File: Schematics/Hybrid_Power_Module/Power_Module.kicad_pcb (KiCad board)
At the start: 4 copper layers, 69.5 x 60 mm, 135 parts, among them J1 ScrewSwitch, J2 Battery, J3 ScrewSwitch, J4 GSE, J5 USB_C_Female_USB2_Small, J6 SWD_B, J7 Stack Male Edge Connector, Q1 AO4447A, Q2 SI2305CDS, Q3 DMN6040SSD-13, SW1 SW_STM_RESET, SW2 SW_STM_BOOT_MODE, U1 TPS61175PWPR, U10 LM66100DCKR, U11 LM66100DCKR, U12 AMS1117-3.3, U13 CP2102N-A02-GQFN20R, U14 STM32F103CBT6, U15 ISO1044BDR, U16 W25Q128JVS, U2 LM74700QDBVRQ1, U3 LM74700QDBVRQ1, U4 ACS37041KLHBLT-010B3, U5 ACS37041KLHBLT-010B5, U6 INA181A2, U7 LMR51430XDDCR, U8 LMR51430XDDCR, U9 LM66100DCKR, Y1 X322516MMB4SI

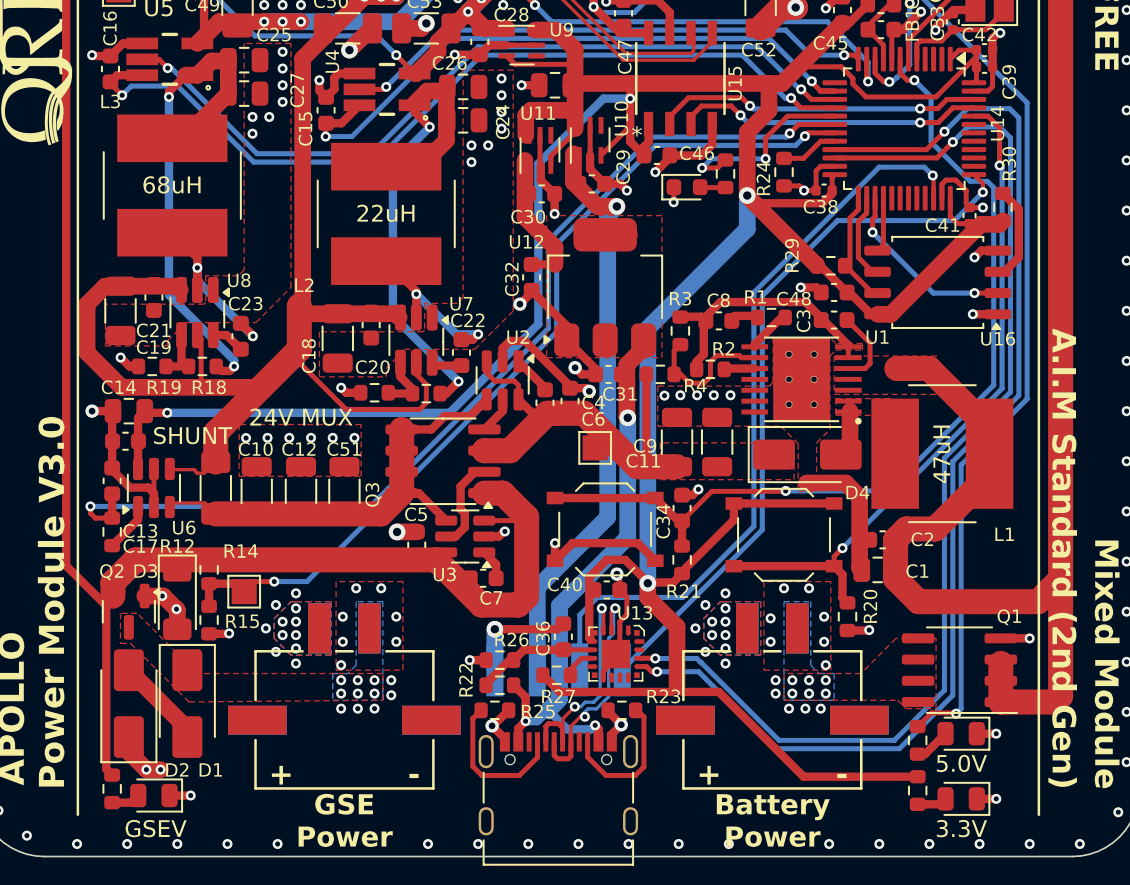
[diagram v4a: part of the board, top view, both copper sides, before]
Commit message: changed current sense and switched to bidirectional TVS for GSE power
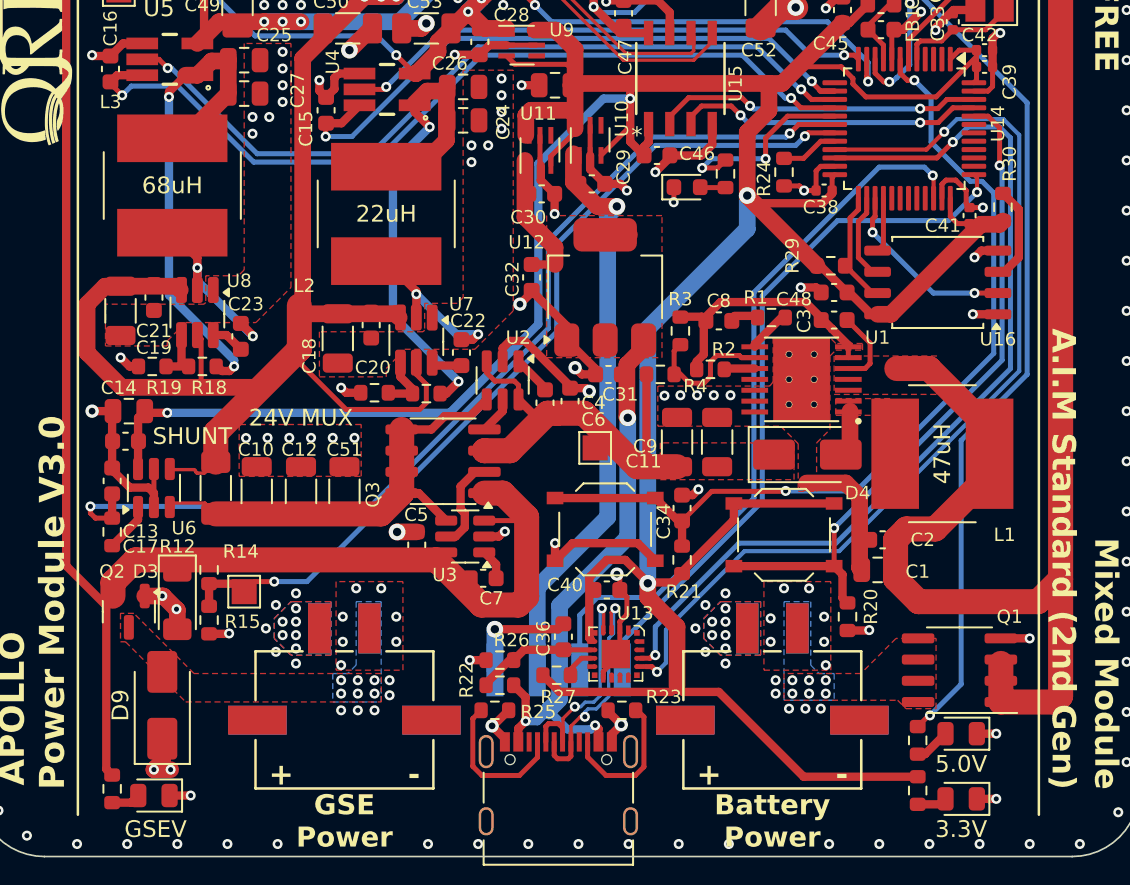
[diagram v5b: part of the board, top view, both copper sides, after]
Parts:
- removed D1, D2: SMAJ30A, Diode_SMD:D_SMA
- added D9: SMAJ30CA, Diode_SMD:D_SMA, F.Cu at (141.3, 90.7)
- U6: value INA181A2 -> INA187A
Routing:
- net USART_RX: track 67.7 -> 55.7 mm
- net USART_TX: track 70.5 -> 58.5 mm
- net Net-(D1-A2): track 4.95 -> 0.00 mm
- net STM_RESET: track 54.1 -> 52.8 mm
- net SWDIO: track 45.3 -> 44.3 mm
- net 5V_PSU: track 125.3 -> 124.4 mm

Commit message: final board submitted to cart
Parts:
- removed C47: 100nF, Capacitor_SMD:C_0603_1608Metric
- TP1: value BATT_GND1 -> GND
- TP13: value GSEV -> 24V.G
- TP2: value GSE_GND1 -> GND
- TP3: value 24V_PSU -> 24V.B
- TP4: value 24V_MUX -> 24V.OR
- TP5: value 5VSENS -> 5V.S
- TP6: value A.S -> B.S
- TP9: value GSE_SENS -> GSE.S
- U15: value ISO1044BDR -> TCAN1051HGVDR
- U16: value W25Q128JVS -> BY25Q128ES
- moved C46 0.32 mm to (171.2, 57.8)
- moved R28 0.30 mm to (175.0, 59.2)
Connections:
- C46 pad 1: 3.3V_MUX -> GND
- C46 pad 2: GND -> 5V_PSU
- U15 pad 1: 3.3V_MUX -> CAN_TX
- U15 pad 2: CAN_TX -> GND
- U15 pad 3: CAN_RX -> 5V_PSU
- U15 pad 4: GND -> CAN_RX
- U15 pad 5: CAN_N -> unconnected-(U15-NC-Pad5)
- U15 pad 6: CAN_P -> CAN_N
- U15 pad 7: GND -> CAN_P
- U15 pad 8: 5V_PSU -> unconnected-(U15-S-Pad8)
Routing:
- net 5V_PSU: track 124.4 -> 133.9 mm, vias 6 -> 8
- net 3.3V_MUX: track 228.1 -> 222.7 mm
- net GND: track 215.1 -> 210.3 mm, vias 195 -> 194
- net CAN_TX: track 19.2 -> 21.2 mm
- net CAN_RX: track 18.0 -> 16.7 mm
- net CAN_N: track 22.0 -> 21.0 mm
- net CAN_P: track 21.9 -> 21.0 mm
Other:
- board text added: "24V.G"
- board text removed: "GSEV"
